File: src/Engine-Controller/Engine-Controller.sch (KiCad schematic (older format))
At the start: 14 parts, among them J1 Jumper_NO, U1 STM32L443VCT6

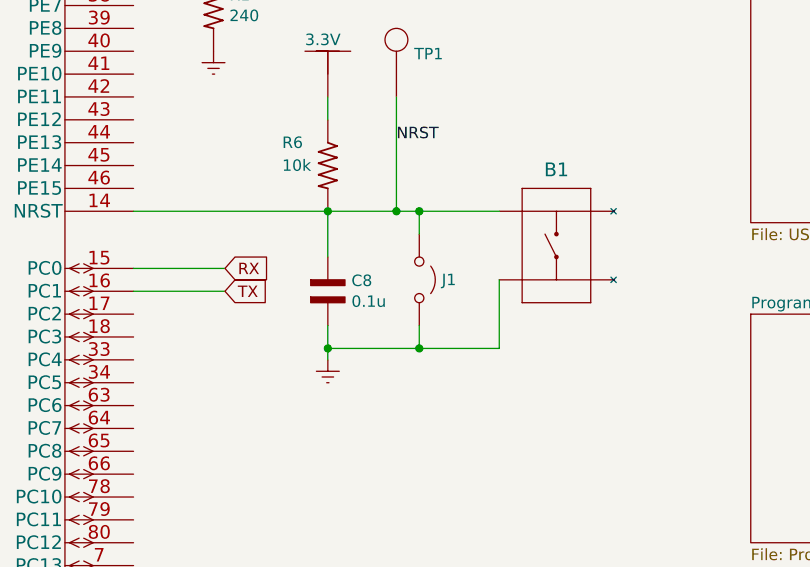
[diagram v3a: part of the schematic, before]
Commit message: Fixed J1 orientation
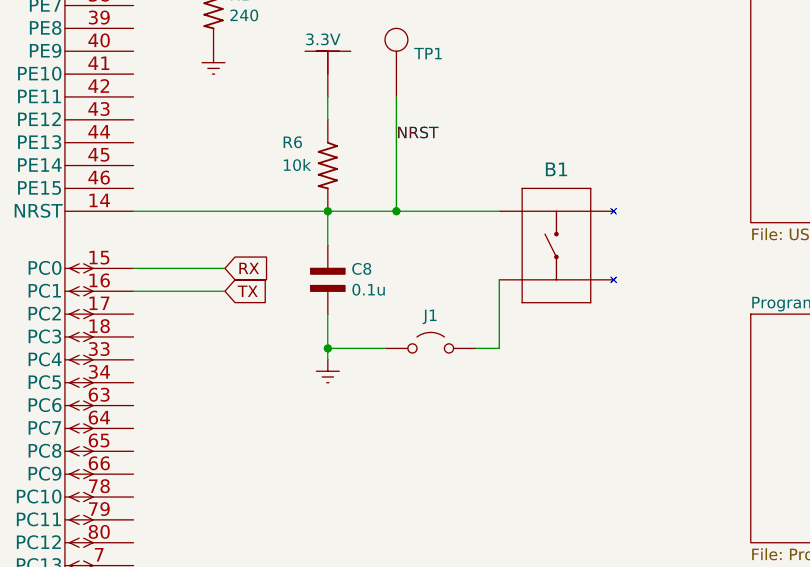
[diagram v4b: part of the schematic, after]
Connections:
- net Earth: now also J1.1 (A); no longer B1.3, J1.2 (B)
- net NRST: no longer J1.1 (A)
- new net: B1.3, J1.2 (B)
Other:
- moved on the sheet: C8, J1
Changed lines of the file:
@@
 L Engine-Controller:CAP_0603 C8
 U 1 1 60DE014C
-P 6250 3450
-F 0 "C8" V 6204 3553 50  0000 L CNN
-F 1 "0.1u" V 6295 3553 50  0000 L CNN
-F 2 "Engine-Controller:CAP_0603" H 6150 3050 50  0001 L BNN
-F 3 "" H 6200 3450 50  0001 L BNN
-	1    6250 3450
+P 6250 3400
+F 0 "C8" V 6204 3503 50  0000 L CNN
+F 1 "0.1u" V 6295 3503 50  0000 L CNN
+F 2 "Engine-Controller:CAP_0603" H 6150 3000 50  0001 L BNN
+F 3 "" H 6200 3400 50  0001 L BNN
+	1    6250 3400
 	0    1    1    0
 $EndComp
@@
 	1    0    0    -1
 $EndComp
-Wire Wire Line
-	6250 3300 6250 3100
-Wire Wire Line
-	6250 3750 6250 3700
 $Comp
 L Engine-Controller:TP TP1
@@
 	6550 2600 6550 3100
 Connection ~ 6550 3100
-Wire Wire Line
-	6550 3100 6650 3100
-Connection ~ 6250 3700
-Wire Wire Line
-	6250 3700 6250 3600
 $Comp
 L Engine-Controller:CAP_0603 C10
@@
 L Engine-Controller:Jumper_NO J1
 U 1 1 6147D8EA
-P 6650 3400
-F 0 "J1" V 6650 3498 50  0000 L CNN
-F 1 "Jumper_NO" H 6650 3310 50  0001 C CNN
-F 2 "" H 6650 3400 50  0001 C CNN
-F 3 "~" H 6650 3400 50  0001 C CNN
-	1    6650 3400
-	0    1    1    0
-$EndComp
-Wire Wire Line
-	6650 3200 6650 3100
-Connection ~ 6650 3100
-Wire Wire Line
-	6650 3600 6650 3700
-Connection ~ 6650 3700
-Wire Wire Line
-	6650 3700 6250 3700
-Wire Wire Line
-	6650 3100 7000 3100
+P 6700 3700
+F 0 "J1" H 6700 3843 50  0000 C CNN
+F 1 "Jumper_NO" H 6700 3610 50  0001 C CNN
+F 2 "" H 6700 3700 50  0001 C CNN
+F 3 "~" H 6700 3700 50  0001 C CNN
+	1    6700 3700
+	1    0    0    -1
+$EndComp
 Wire Wire Line
 	7000 3700 7000 3400
 Wire Wire Line
-	6650 3700 7000 3700
+	6550 3100 7000 3100
+Wire Wire Line
+	6900 3700 7000 3700
+Wire Wire Line
+	6500 3700 6250 3700
+Connection ~ 6250 3700
+Wire Wire Line
+	6250 3700 6250 3750
+Wire Wire Line
+	6250 3550 6250 3700
+Wire Wire Line
+	6250 3250 6250 3100
 $EndSCHEMATC

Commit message: Added Flash
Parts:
- added C14, C15: 0.1u, symbol Engine-Controller:CAP_0603
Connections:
- net 3.3V: now also C14.2, C15.2
- net Earth: now also C14.1, C15.1
- net FLASH_MISO: now reaches U1.17 (PC2)
- net FLASH_MOSI: now reaches U1.18 (PC3)
- net FLASH_SCK: now reaches U1.47 (PB10)
- net FLASH_SS: now reaches U1.51 (PB12)
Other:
- moved on the sheet: C10, C11, C12, C13, C9
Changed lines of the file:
@@
 $Descr A4 11693 8268
 encoding utf-8
-Sheet 1 5
+Sheet 1 6
 Title "Engine Controller Microcontroller Board"
 Date "2021-06-26"
@@
 $EndDescr
 $Sheet
-S 8100 750  2850 1050
+S 8200 650  2850 1050
 U 60D7F309
 F0 "power" 50
@@
 $EndSheet
 $Sheet
-S 8100 2150 2850 1000
+S 9700 2050 1300 1100
 U 60DAA9B3
 F0 "USB" 50
@@
 L power:Earth #PWR0101
 U 1 1 60F20D33
-P 2750 3200
-F 0 "#PWR0101" H 2750 2950 50  0001 C CNN
-F 1 "Earth" H 2750 3050 50  0001 C CNN
-F 2 "" H 2750 3200 50  0001 C CNN
-F 3 "~" H 2750 3200 50  0001 C CNN
-	1    2750 3200
+P 2750 3100
+F 0 "#PWR0101" H 2750 2850 50  0001 C CNN
+F 1 "Earth" H 2750 2950 50  0001 C CNN
+F 2 "" H 2750 3100 50  0001 C CNN
+F 3 "~" H 2750 3100 50  0001 C CNN
+	1    2750 3100
 	1    0    0    -1
 $EndComp
@@
 L Engine-Controller:CAP_0603 C10
 U 1 1 61273C95
-P 1050 2950
-F 0 "C10" V 1004 3053 50  0000 L CNN
-F 1 "0.1u" V 1095 3053 50  0000 L CNN
-F 2 "" H 950 2550 50  0001 L BNN
-F 3 "" H 1000 2950 50  0001 L BNN
-	1    1050 2950
+P 1050 2150
+F 0 "C10" V 1004 2253 50  0000 L CNN
+F 1 "0.1u" V 1095 2253 50  0000 L CNN
+F 2 "" H 950 1750 50  0001 L BNN
+F 3 "" H 1000 2150 50  0001 L BNN
+	1    1050 2150
 	0    1    1    0
 $EndComp
@@
 L Engine-Controller:CAP_0603 C11
 U 1 1 6127C459
-P 1400 2950
-F 0 "C11" V 1354 3053 50  0000 L CNN
-F 1 "0.1u" V 1445 3053 50  0000 L CNN
-F 2 "" H 1300 2550 50  0001 L BNN
-F 3 "" H 1350 2950 50  0001 L BNN
-	1    1400 2950
+P 1400 2150
+F 0 "C11" V 1354 2253 50  0000 L CNN
+F 1 "0.1u" V 1445 2253 50  0000 L CNN
+F 2 "" H 1300 1750 50  0001 L BNN
+F 3 "" H 1350 2150 50  0001 L BNN
+	1    1400 2150
 	0    1    1    0
 $EndComp
@@
 L Engine-Controller:CAP_0603 C12
 U 1 1 6127D073
-P 1750 2950
-F 0 "C12" V 1704 3053 50  0000 L CNN
-F 1 "0.1u" V 1795 3053 50  0000 L CNN
-F 2 "" H 1650 2550 50  0001 L BNN
-F 3 "" H 1700 2950 50  0001 L BNN
-	1    1750 2950
+P 1750 2150
+F 0 "C12" V 1704 2253 50  0000 L CNN
+F 1 "0.1u" V 1795 2253 50  0000 L CNN
+F 2 "" H 1650 1750 50  0001 L BNN
+F 3 "" H 1700 2150 50  0001 L BNN
+	1    1750 2150
 	0    1    1    0
 $EndComp
@@
 L Engine-Controller:CAP_0603 C13
 U 1 1 6127DC78
-P 2100 2950
-F 0 "C13" V 2054 3053 50  0000 L CNN
-F 1 "0.1u" V 2145 3053 50  0000 L CNN
-F 2 "" H 2000 2550 50  0001 L BNN
-F 3 "" H 2050 2950 50  0001 L BNN
-	1    2100 2950
+P 2100 2150
+F 0 "C13" V 2054 2253 50  0000 L CNN
+F 1 "0.1u" V 2145 2253 50  0000 L CNN
+F 2 "" H 2000 1750 50  0001 L BNN
+F 3 "" H 2050 2150 50  0001 L BNN
+	1    2100 2150
 	0    1    1    0
 $EndComp
@@
 L Engine-Controller:CAP_0603 C9
 U 1 1 6127EE14
-P 700 2950
-F 0 "C9" V 654 3053 50  0000 L CNN
-F 1 "0.1u" V 745 3053 50  0000 L CNN
-F 2 "" H 600 2550 50  0001 L BNN
-F 3 "" H 650 2950 50  0001 L BNN
-	1    700  2950
-	0    1    1    0
-$EndComp
-Wire Wire Line
-	2550 2800 2100 2800
-Connection ~ 2550 2800
-Connection ~ 1050 2800
-Wire Wire Line
-	1050 2800 700  2800
-Connection ~ 1400 2800
-Wire Wire Line
-	1400 2800 1050 2800
-Connection ~ 1750 2800
-Wire Wire Line
-	1750 2800 1400 2800
-Connection ~ 2100 2800
-Wire Wire Line
-	2100 2800 1750 2800
-Wire Wire Line
-	700  3100 1050 3100
-Connection ~ 2750 3100
-Wire Wire Line
-	2750 3100 2750 3200
-Connection ~ 1050 3100
-Wire Wire Line
-	1050 3100 1400 3100
-Connection ~ 1400 3100
-Wire Wire Line
-	1400 3100 1750 3100
-Connection ~ 1750 3100
-Wire Wire Line
-	1750 3100 2100 3100
-Connection ~ 2100 3100
-Wire Wire Line
-	2100 3100 2750 3100
-Text Notes 900  2700 0    50   ~ 0
+P 700 2150
+F 0 "C9" V 654 2253 50  0000 L CNN
+F 1 "0.1u" V 745 2253 50  0000 L CNN
+F 2 "" H 600 1750 50  0001 L BNN
+F 3 "" H 650 2150 50  0001 L BNN
+	1    700  2150
+	0    1    1    0
+$EndComp
+Wire Wire Line
+	2550 2000 2100 2000
+Connection ~ 1050 2000
+Wire Wire Line
+	1050 2000 700  2000
+Connection ~ 1400 2000
+Wire Wire Line
+	1400 2000 1050 2000
+Connection ~ 1750 2000
+Wire Wire Line
+	1750 2000 1400 2000
+Connection ~ 2100 2000
+Wire Wire Line
+	2100 2000 1750 2000
+Wire Wire Line
+	700  2300 1050 2300
+Connection ~ 1050 2300
+Wire Wire Line
+	1050 2300 1400 2300
+Connection ~ 1400 2300
+Wire Wire Line
+	1400 2300 1750 2300
+Connection ~ 1750 2300
+Wire Wire Line
+	1750 2300 2100 2300
+Connection ~ 2100 2300
+Wire Wire Line
+	2100 2300 2750 2300
+Text Notes 900  1900 0    50   ~ 0
 Microcontroller Decoupling Caps
 Text Label 6550 2800 0    50   ~ 0
@@
 Wire Wire Line
 	6250 3250 6250 3100
+$Comp
+L Engine-Controller:CAP_0603 C14
+U 1 1 6159BC7F
+P 1700 2750
+F 0 "C14" V 1654 2853 50  0000 L CNN
+F 1 "0.1u" V 1745 2853 50  0000 L CNN
+F 2 "" H 1600 2350 50  0001 L BNN
+F 3 "" H 1650 2750 50  0001 L BNN
+	1    1700 2750
+	0    1    1    0
+$EndComp
+$Comp
+L Engine-Controller:CAP_0603 C15
+U 1 1 6159CF33
+P 2050 2750
+F 0 "C15" V 2004 2853 50  0000 L CNN
+F 1 "0.1u" V 2095 2853 50  0000 L CNN
+F 2 "" H 1950 2350 50  0001 L BNN
+F 3 "" H 2000 2750 50  0001 L BNN
+	1    2050 2750
+	0    1    1    0
+$EndComp
+Wire Wire Line
+	1700 2600 2050 2600
+Connection ~ 2050 2600
+Wire Wire Line
+	2050 2600 2550 2600
+Wire Wire Line
+	1700 2900 2050 2900
+Connection ~ 2050 2900
+Wire Wire Line
+	2050 2900 2750 2900
+Text GLabel 2700 6100 0    50   Input ~ 0
+FLASH_SCK
+Wire Wire Line
+	3000 6100 2700 6100
+Text GLabel 5550 3550 2    50   Input ~ 0
+FLASH_MISO
+Wire Wire Line
+	5550 3550 5400 3550
+Text GLabel 5550 3650 2    50   Input ~ 0
+FLASH_MOSI
+Wire Wire Line
+	5550 3650 5400 3650
+Text GLabel 2650 6300 0    50   Input ~ 0
+FLASH_SS
+Wire Wire Line
+	3000 6300 2650 6300
+$Sheet
+S 8100 2000 1350 1150
+U 6177D07C
+F0 "Flash_SD" 50
+F1 "Flash_SD.sch" 50
+$EndSheet
 $EndSCHEMATC

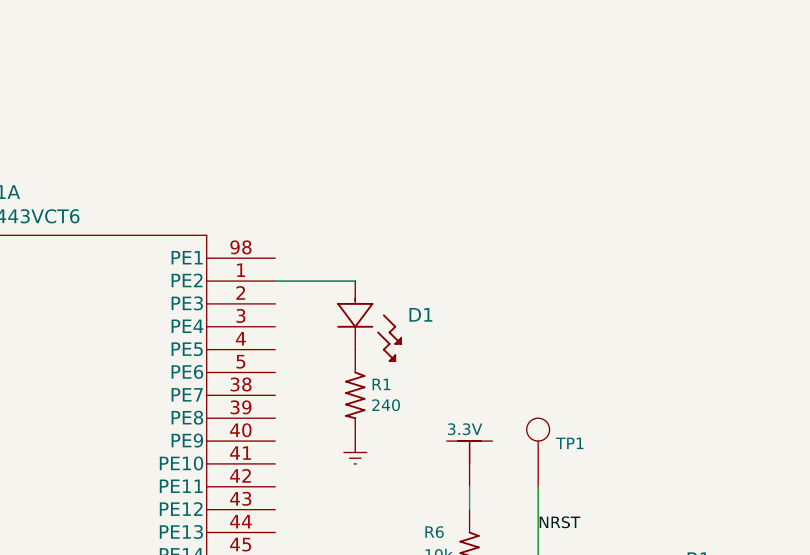
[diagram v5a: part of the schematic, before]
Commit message: Added Micro SD Card
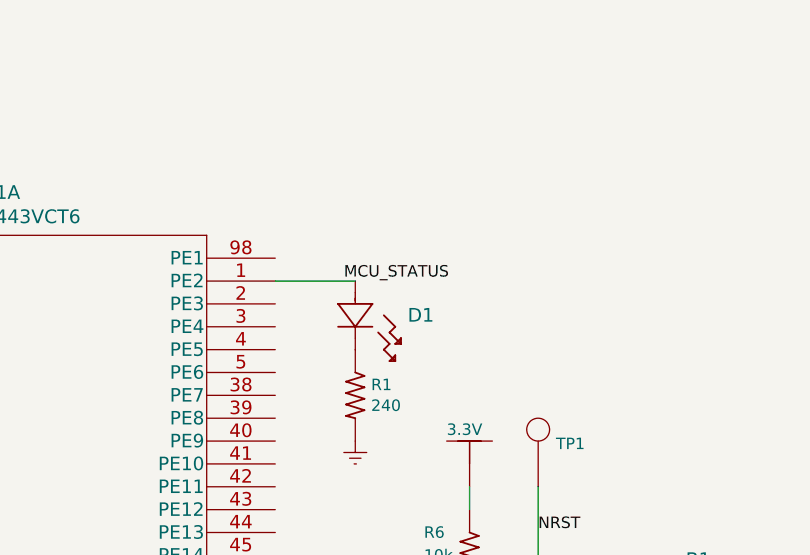
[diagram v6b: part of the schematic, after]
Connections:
- net MCU_STATUS: now reaches D1.2, U1.1 (PE2)
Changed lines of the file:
@@
 F1 "Flash_SD.sch" 50
 $EndSheet
+Text Label 5700 1700 0    50   ~ 0
+MCU_STATUS
 $EndSCHEMATC

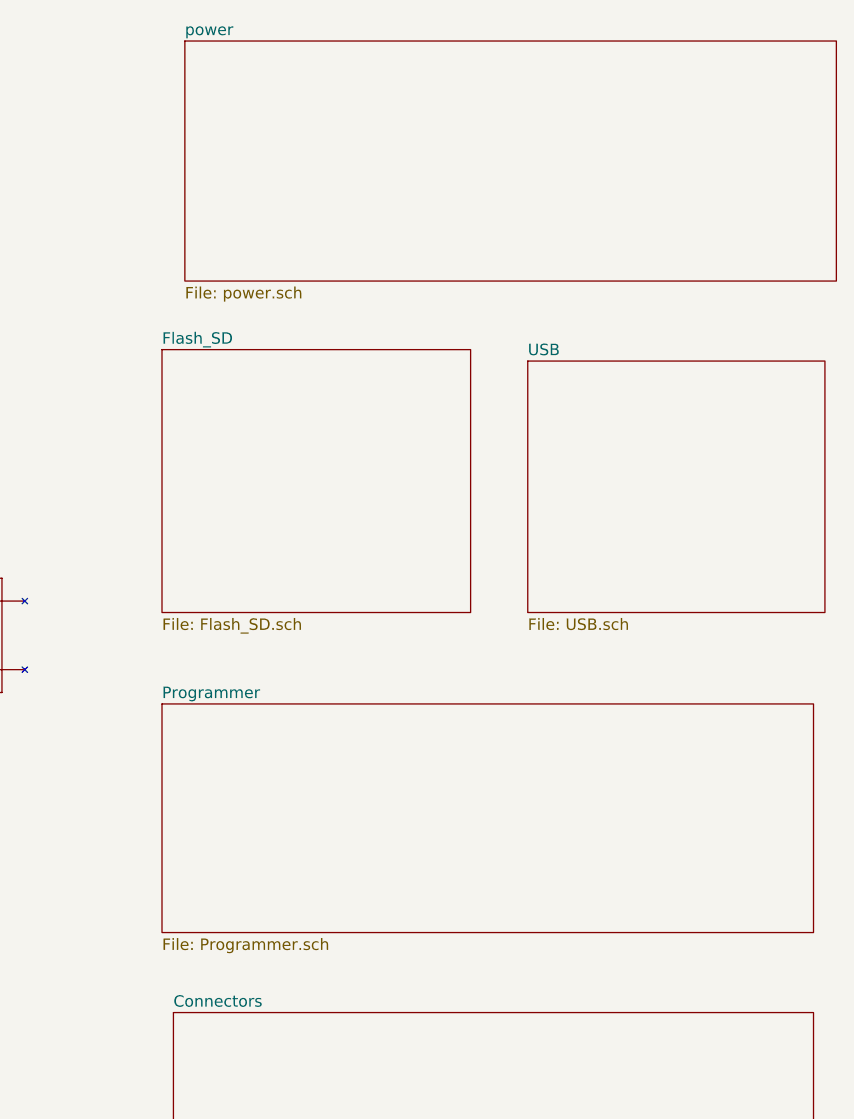
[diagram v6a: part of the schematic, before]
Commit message: Moved Programmer to connectors sheet
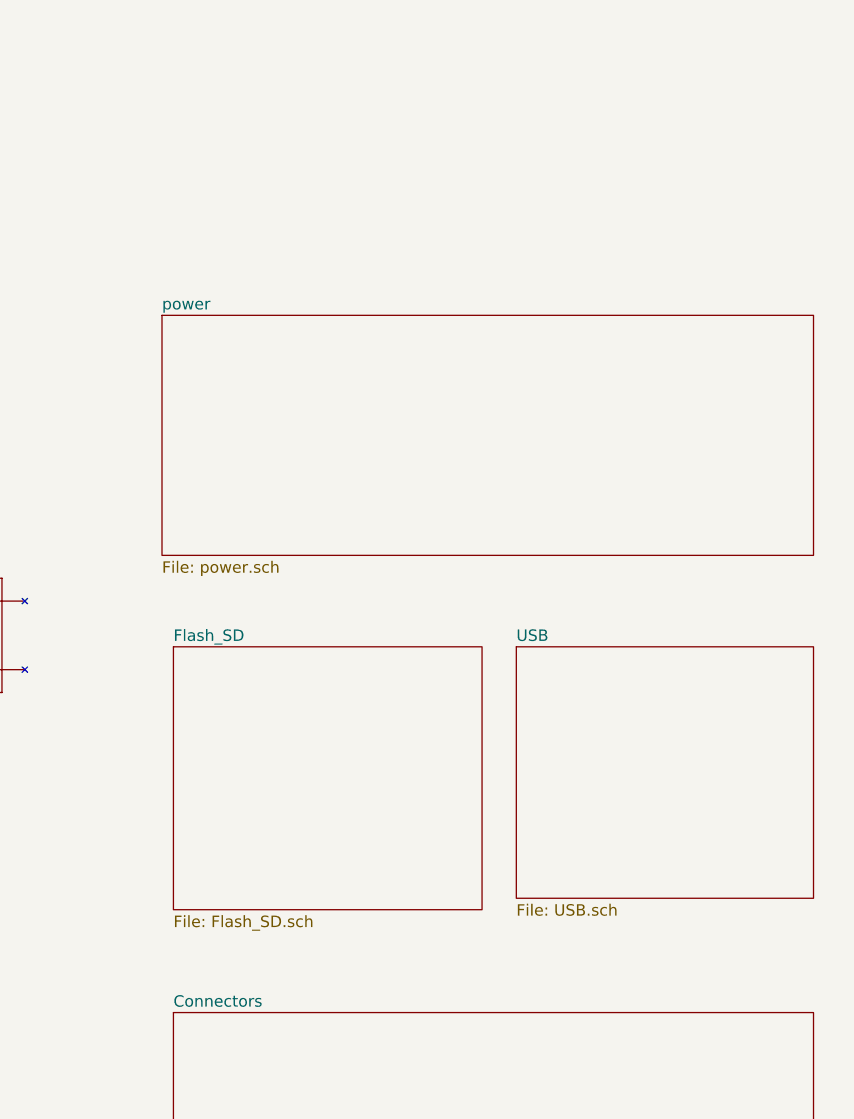
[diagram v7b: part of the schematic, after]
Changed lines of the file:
@@
 $Descr A4 11693 8268
 encoding utf-8
-Sheet 1 6
+Sheet 1 5
 Title "Engine Controller Microcontroller Board"
 Date "2021-06-26"
@@
 $EndDescr
 $Sheet
-S 8200 650  2850 1050
+S 8100 1850 2850 1050
 U 60D7F309
 F0 "power" 50
@@
 $EndSheet
 $Sheet
-S 9700 2050 1300 1100
+S 9650 3300 1300 1100
 U 60DAA9B3
 F0 "USB" 50
 F1 "USB.sch" 50
-$EndSheet
-$Sheet
-S 8100 3550 2850 1000
-U 60DAAA3E
-F0 "Programmer" 50
-F1 "Programmer.sch" 50
 $EndSheet
 $Comp
@@
 	3000 6300 2650 6300
 $Sheet
-S 8100 2000 1350 1150
+S 8150 3300 1350 1150
 U 6177D07C
 F0 "Flash_SD" 50
